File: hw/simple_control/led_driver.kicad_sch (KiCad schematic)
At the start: 11 parts, among them U1 SN74AHCT125D

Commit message: [hw] Complete root schematics of simple control
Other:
- company: (none) -> Stefan Misik
- title: (none) -> WS2812 Simple Controller
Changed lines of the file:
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@@
 (kicad_sch (version 20230121) (generator eeschema)
   (paper "A4")
+  (title_block
+    (title "WS2812 Simple Controller")
+    (date "2023-03-09")
+    (company "Stefan Misik")
+    (comment 1 "LED Data Driver")
+  )
   (junction (at 88.9 139.7) (diameter 0) (color 0 0 0 0)
   )

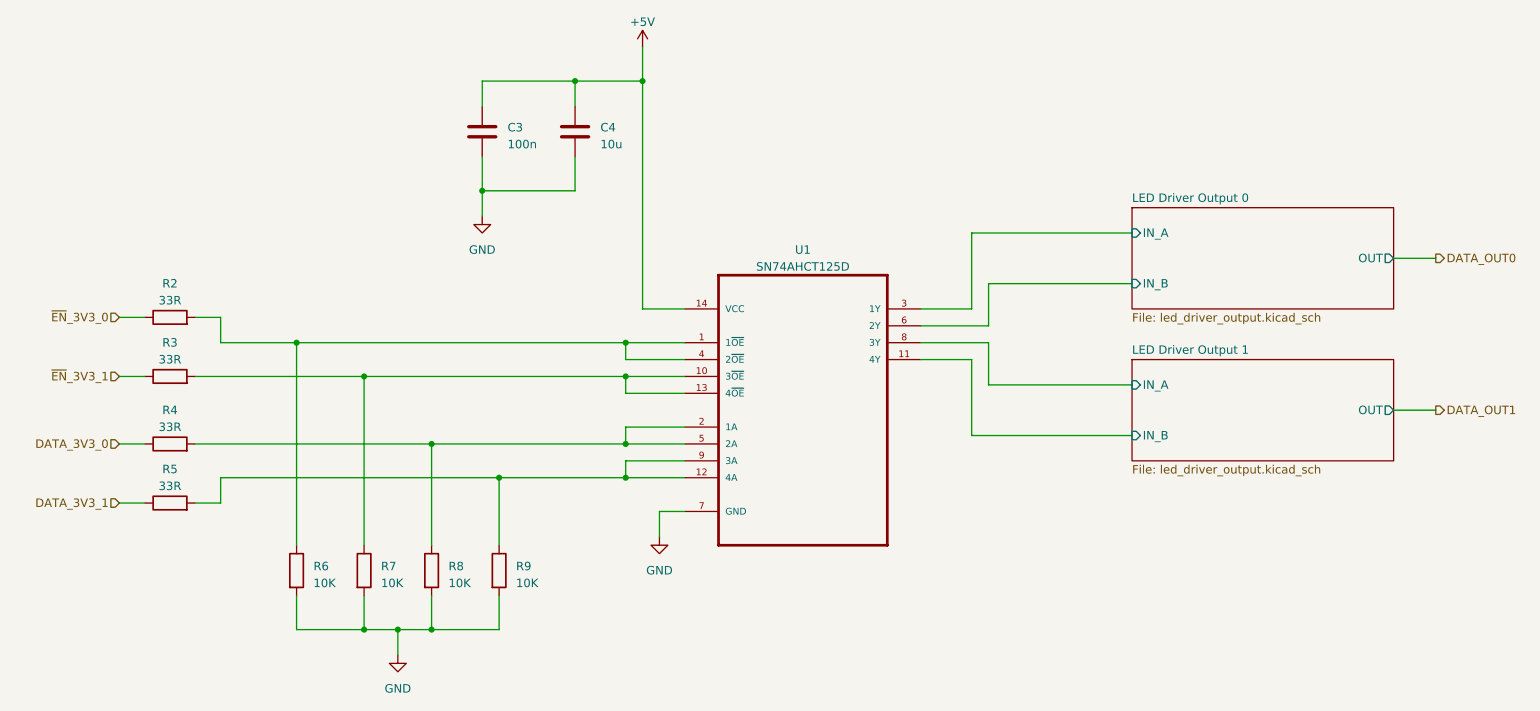
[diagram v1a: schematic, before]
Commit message: [hw] Wire some RPi Pico/Zero connections
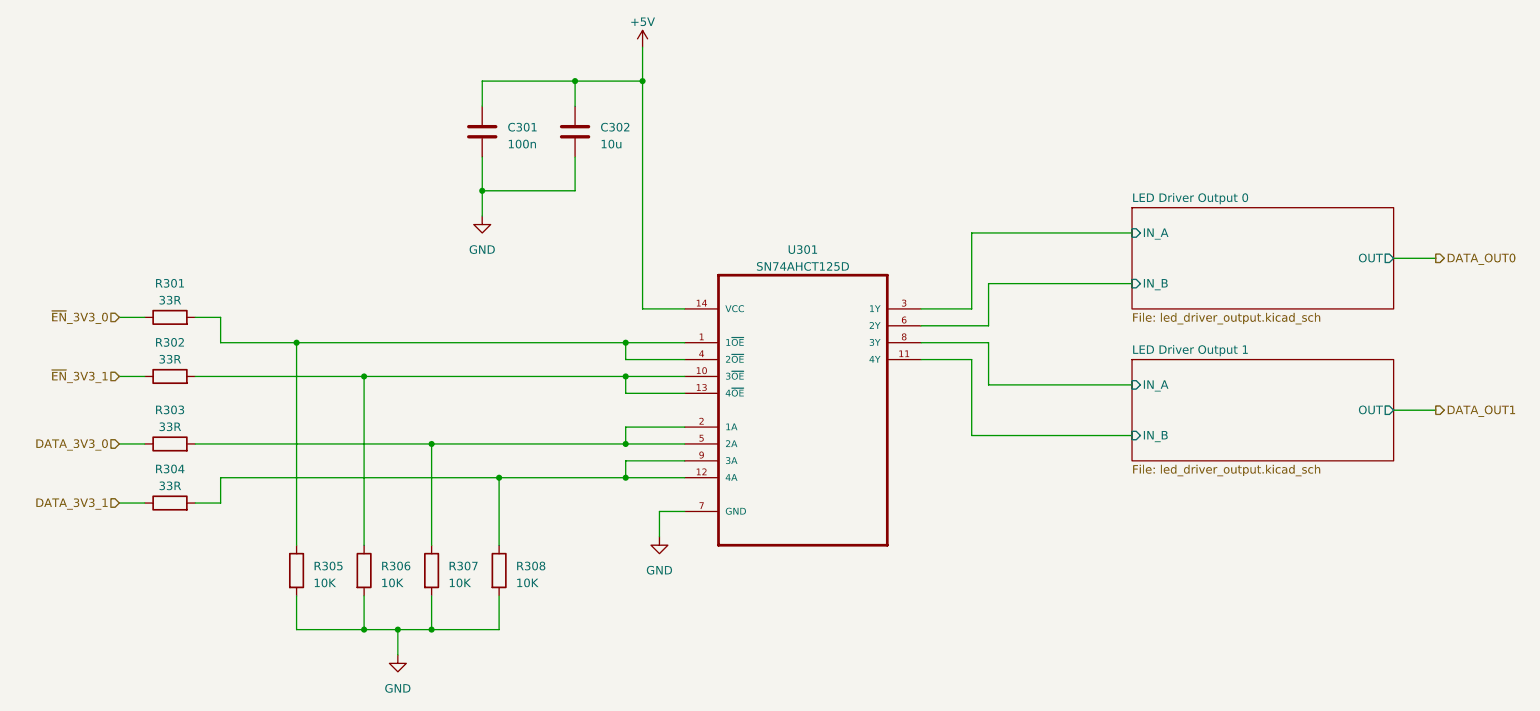
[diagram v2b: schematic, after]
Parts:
- renumbered C3 to C301, C4 to C302, R2 to R301, R3 to R302, R4 to R303, R5 to R304, R6 to R305, R7 to R306, R8 to R307, R9 to R308, U1 to U301
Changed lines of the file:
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@@
   (symbol (lib_id "Device:C") (at 110.49 64.77 0) (unit 1)
     (in_bom yes) (on_board yes) (dnp no) (fields_autoplaced)
-    (property "Reference" "C4" (at 114.3 64.135 0)
+    (property "Reference" "C302" (at 114.3 64.135 0)
       (effects (font (size 1.27 1.27)) (justify left))
     )
@@
       (project "simple_control"
         (path "/063164e8-0d2a-492b-8a61-e4fa4fbf06a6/3fe7738b-ee8c-4030-a832-f1998a82ba48"
-          (reference "C4") (unit 1)
+          (reference "C302") (unit 1)
         )
       )
@@
   (symbol (lib_id "Device:R") (at 68.58 130.81 0) (unit 1)
     (in_bom yes) (on_board yes) (dnp no) (fields_autoplaced)
-    (property "Reference" "R6" (at 71.12 130.175 0)
+    (property "Reference" "R305" (at 71.12 130.175 0)
       (effects (font (size 1.27 1.27)) (justify left))
     )
@@
       (project "simple_control"
         (path "/063164e8-0d2a-492b-8a61-e4fa4fbf06a6/3fe7738b-ee8c-4030-a832-f1998a82ba48"
-          (reference "R6") (unit 1)
+          (reference "R305") (unit 1)
         )
       )
@@
   (symbol (lib_id "Device:R") (at 49.53 101.6 90) (unit 1)
     (in_bom yes) (on_board yes) (dnp no) (fields_autoplaced)
-    (property "Reference" "R3" (at 49.53 96.52 90)
+    (property "Reference" "R302" (at 49.53 96.52 90)
       (effects (font (size 1.27 1.27)))
     )
@@
       (project "simple_control"
         (path "/063164e8-0d2a-492b-8a61-e4fa4fbf06a6/3fe7738b-ee8c-4030-a832-f1998a82ba48"
-          (reference "R3") (unit 1)
+          (reference "R302") (unit 1)
         )
       )
@@
   (symbol (lib_id "Device:R") (at 49.53 92.71 90) (unit 1)
     (in_bom yes) (on_board yes) (dnp no) (fields_autoplaced)
-    (property "Reference" "R2" (at 49.53 87.63 90)
+    (property "Reference" "R301" (at 49.53 87.63 90)
       (effects (font (size 1.27 1.27)))
     )
@@
       (project "simple_control"
         (path "/063164e8-0d2a-492b-8a61-e4fa4fbf06a6/3fe7738b-ee8c-4030-a832-f1998a82ba48"
-          (reference "R2") (unit 1)
+          (reference "R301") (unit 1)
         )
       )
@@
   (symbol (lib_id "Device:R") (at 99.06 130.81 0) (unit 1)
     (in_bom yes) (on_board yes) (dnp no) (fields_autoplaced)
-    (property "Reference" "R9" (at 101.6 130.175 0)
+    (property "Reference" "R308" (at 101.6 130.175 0)
       (effects (font (size 1.27 1.27)) (justify left))
     )
@@
       (project "simple_control"
         (path "/063164e8-0d2a-492b-8a61-e4fa4fbf06a6/3fe7738b-ee8c-4030-a832-f1998a82ba48"
-          (reference "R9") (unit 1)
+          (reference "R308") (unit 1)
         )
       )
@@
   (symbol (lib_id "Device:C") (at 96.52 64.77 0) (unit 1)
     (in_bom yes) (on_board yes) (dnp no) (fields_autoplaced)
-    (property "Reference" "C3" (at 100.33 64.135 0)
+    (property "Reference" "C301" (at 100.33 64.135 0)
       (effects (font (size 1.27 1.27)) (justify left))
     )
@@
       (project "simple_control"
         (path "/063164e8-0d2a-492b-8a61-e4fa4fbf06a6/3fe7738b-ee8c-4030-a832-f1998a82ba48"
-          (reference "C3") (unit 1)
+          (reference "C301") (unit 1)
         )
       )
@@
   (symbol (lib_id "sn74ahct125d:SN74AHCT125D") (at 144.78 104.14 0) (unit 1)
     (in_bom yes) (on_board yes) (dnp no) (fields_autoplaced)
-    (property "Reference" "U1" (at 144.78 82.55 0)
+    (property "Reference" "U301" (at 144.78 82.55 0)
       (effects (font (size 1.27 1.27)))
     )
@@
       (project "simple_control"
         (path "/063164e8-0d2a-492b-8a61-e4fa4fbf06a6/3fe7738b-ee8c-4030-a832-f1998a82ba48"
-          (reference "U1") (unit 1)
+          (reference "U301") (unit 1)
         )
       )
@@
   (symbol (lib_id "power:GND") (at 83.82 143.51 0) (unit 1)
     (in_bom yes) (on_board yes) (dnp no) (fields_autoplaced)
-    (property "Reference" "#PWR06" (at 83.82 149.86 0)
+    (property "Reference" "#PWR0304" (at 83.82 149.86 0)
       (effects (font (size 1.27 1.27)) hide)
     )
@@
       (project "simple_control"
         (path "/063164e8-0d2a-492b-8a61-e4fa4fbf06a6/3fe7738b-ee8c-4030-a832-f1998a82ba48"
-          (reference "#PWR06") (unit 1)
+          (reference "#PWR0304") (unit 1)
         )
       )
@@
   (symbol (lib_id "power:GND") (at 123.19 125.73 0) (unit 1)
     (in_bom yes) (on_board yes) (dnp no) (fields_autoplaced)
-    (property "Reference" "#PWR05" (at 123.19 132.08 0)
+    (property "Reference" "#PWR0303" (at 123.19 132.08 0)
       (effects (font (size 1.27 1.27)) hide)
     )
@@
       (project "simple_control"
         (path "/063164e8-0d2a-492b-8a61-e4fa4fbf06a6/3fe7738b-ee8c-4030-a832-f1998a82ba48"
-          (reference "#PWR05") (unit 1)
+          (reference "#PWR0303") (unit 1)
         )
       )
@@
   (symbol (lib_id "Device:R") (at 88.9 130.81 0) (unit 1)
     (in_bom yes) (on_board yes) (dnp no) (fields_autoplaced)
-    (property "Reference" "R8" (at 91.44 130.175 0)
+    (property "Reference" "R307" (at 91.44 130.175 0)
       (effects (font (size 1.27 1.27)) (justify left))
     )
@@
       (project "simple_control"
         (path "/063164e8-0d2a-492b-8a61-e4fa4fbf06a6/3fe7738b-ee8c-4030-a832-f1998a82ba48"
-          (reference "R8") (unit 1)
+          (reference "R307") (unit 1)
         )
       )
@@
   (symbol (lib_id "Device:R") (at 49.53 120.65 90) (unit 1)
     (in_bom yes) (on_board yes) (dnp no) (fields_autoplaced)
-    (property "Reference" "R5" (at 49.53 115.57 90)
+    (property "Reference" "R304" (at 49.53 115.57 90)
       (effects (font (size 1.27 1.27)))
     )
@@
       (project "simple_control"
         (path "/063164e8-0d2a-492b-8a61-e4fa4fbf06a6/3fe7738b-ee8c-4030-a832-f1998a82ba48"
-          (reference "R5") (unit 1)
+          (reference "R304") (unit 1)
         )
       )
@@
   (symbol (lib_id "Device:R") (at 49.53 111.76 90) (unit 1)
     (in_bom yes) (on_board yes) (dnp no) (fields_autoplaced)
-    (property "Reference" "R4" (at 49.53 106.68 90)
+    (property "Reference" "R303" (at 49.53 106.68 90)
       (effects (font (size 1.27 1.27)))
     )
@@
       (project "simple_control"
         (path "/063164e8-0d2a-492b-8a61-e4fa4fbf06a6/3fe7738b-ee8c-4030-a832-f1998a82ba48"
-          (reference "R4") (unit 1)
+          (reference "R303") (unit 1)
         )
       )
@@
   (symbol (lib_id "power:GND") (at 96.52 77.47 0) (unit 1)
     (in_bom yes) (on_board yes) (dnp no) (fields_autoplaced)
-    (property "Reference" "#PWR04" (at 96.52 83.82 0)
+    (property "Reference" "#PWR0302" (at 96.52 83.82 0)
       (effects (font (size 1.27 1.27)) hide)
     )
@@
       (project "simple_control"
         (path "/063164e8-0d2a-492b-8a61-e4fa4fbf06a6/3fe7738b-ee8c-4030-a832-f1998a82ba48"
-          (reference "#PWR04") (unit 1)
+          (reference "#PWR0302") (unit 1)
         )
       )
@@
   (symbol (lib_id "Device:R") (at 78.74 130.81 0) (unit 1)
     (in_bom yes) (on_board yes) (dnp no) (fields_autoplaced)
-    (property "Reference" "R7" (at 81.28 130.175 0)
+    (property "Reference" "R306" (at 81.28 130.175 0)
       (effects (font (size 1.27 1.27)) (justify left))
     )
@@
       (project "simple_control"
         (path "/063164e8-0d2a-492b-8a61-e4fa4fbf06a6/3fe7738b-ee8c-4030-a832-f1998a82ba48"
-          (reference "R7") (unit 1)
+          (reference "R306") (unit 1)
         )
       )
@@
   (symbol (lib_id "power:+5V") (at 120.65 52.07 0) (unit 1)
     (in_bom yes) (on_board yes) (dnp no) (fields_autoplaced)
-    (property "Reference" "#PWR03" (at 120.65 55.88 0)
+    (property "Reference" "#PWR0301" (at 120.65 55.88 0)
       (effects (font (size 1.27 1.27)) hide)
     )
@@
       (project "simple_control"
         (path "/063164e8-0d2a-492b-8a61-e4fa4fbf06a6/3fe7738b-ee8c-4030-a832-f1998a82ba48"
-          (reference "#PWR03") (unit 1)
-        )
-      )
+          (reference "#PWR0301") (unit 1)
+        )
+      )

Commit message: chore(hw): assign footprints
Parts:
- C301: footprint (none) -> Capacitor_SMD:C_0805_2012Metric_Pad1.18x1.45mm_HandSolder
- C302: footprint (none) -> Capacitor_SMD:C_1206_3216Metric_Pad1.33x1.80mm_HandSolder
- R301, R302, R303, R304, R305, R306, R307, R308: footprint (none) -> Resistor_SMD:R_0805_2012Metric_Pad1.20x1.40mm_HandSolder
- U301: footprint SOIC127P600X175-14N -> Package_SO:SOIC-14_3.9x8.7mm_P1.27mm
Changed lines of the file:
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@@
       (effects (font (size 1.27 1.27)) (justify left))
     )
-    (property "Footprint" "" (at 111.4552 68.58 0)
+    (property "Footprint" "Capacitor_SMD:C_1206_3216Metric_Pad1.33x1.80mm_HandSolder" (at 111.4552 68.58 0)
       (effects (font (size 1.27 1.27)) hide)
     )
@@
       (effects (font (size 1.27 1.27)) (justify left))
     )
-    (property "Footprint" "" (at 66.802 130.81 90)
+    (property "Footprint" "Resistor_SMD:R_0805_2012Metric_Pad1.20x1.40mm_HandSolder" (at 66.802 130.81 90)
       (effects (font (size 1.27 1.27)) hide)
     )
@@
       (effects (font (size 1.27 1.27)))
     )
-    (property "Footprint" "" (at 49.53 103.378 90)
+    (property "Footprint" "Resistor_SMD:R_0805_2012Metric_Pad1.20x1.40mm_HandSolder" (at 49.53 103.378 90)
       (effects (font (size 1.27 1.27)) hide)
     )
@@
       (effects (font (size 1.27 1.27)))
     )
-    (property "Footprint" "" (at 49.53 94.488 90)
+    (property "Footprint" "Resistor_SMD:R_0805_2012Metric_Pad1.20x1.40mm_HandSolder" (at 49.53 94.488 90)
       (effects (font (size 1.27 1.27)) hide)
     )
@@
       (effects (font (size 1.27 1.27)) (justify left))
     )
-    (property "Footprint" "" (at 97.282 130.81 90)
+    (property "Footprint" "Resistor_SMD:R_0805_2012Metric_Pad1.20x1.40mm_HandSolder" (at 97.282 130.81 90)
       (effects (font (size 1.27 1.27)) hide)
     )
@@
       (effects (font (size 1.27 1.27)) (justify left))
     )
-    (property "Footprint" "" (at 97.4852 68.58 0)
+    (property "Footprint" "Capacitor_SMD:C_0805_2012Metric_Pad1.18x1.45mm_HandSolder" (at 97.4852 68.58 0)
       (effects (font (size 1.27 1.27)) hide)
     )
@@
       (effects (font (size 1.27 1.27)))
     )
-    (property "Footprint" "SOIC127P600X175-14N" (at 144.78 104.14 0)
+    (property "Footprint" "Package_SO:SOIC-14_3.9x8.7mm_P1.27mm" (at 144.78 104.14 0)
       (effects (font (size 1.27 1.27)) (justify left bottom) hide)
     )
@@
       (effects (font (size 1.27 1.27)) (justify left))
     )
-    (property "Footprint" "" (at 87.122 130.81 90)
+    (property "Footprint" "Resistor_SMD:R_0805_2012Metric_Pad1.20x1.40mm_HandSolder" (at 87.122 130.81 90)
       (effects (font (size 1.27 1.27)) hide)
     )
@@
       (effects (font (size 1.27 1.27)))
     )
-    (property "Footprint" "" (at 49.53 122.428 90)
+    (property "Footprint" "Resistor_SMD:R_0805_2012Metric_Pad1.20x1.40mm_HandSolder" (at 49.53 122.428 90)
       (effects (font (size 1.27 1.27)) hide)
     )
@@
       (effects (font (size 1.27 1.27)))
     )
-    (property "Footprint" "" (at 49.53 113.538 90)
+    (property "Footprint" "Resistor_SMD:R_0805_2012Metric_Pad1.20x1.40mm_HandSolder" (at 49.53 113.538 90)
       (effects (font (size 1.27 1.27)) hide)
     )
@@
       (effects (font (size 1.27 1.27)) (justify left))
     )
-    (property "Footprint" "" (at 76.962 130.81 90)
-      (effects (font (size 1.27 1.27)) hide)
-    )
+    (property "Footprint" "Resistor_SMD:R_0805_2012Metric_Pad1.20x1.40mm_HandSolder" (at 76.962 130.81 90)
+      (effects (font (size 1.27 1.27)) hide)
+    )

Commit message: chore(hw): minor layout fixes, add notes
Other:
- note added: "It should be possible to use pin-compatible 74AHC125 from keypad buffer here"
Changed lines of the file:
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@@
     (stroke (width 0) (type default))
+  )
+  (text "It should be possible to use pin-compatible \n74AHC125 from keypad buffer here"
+    (at 125.73 78.74 0)
+    (effects (font (size 1.27 1.27)) (justify left bottom))
   )
   (hierarchical_label "~{EN}_3V3_0" (shape input) (at 41.91 92.71 180) (fields_autoplaced)
